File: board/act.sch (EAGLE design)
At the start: 27 parts, among them IC1 7805T, U1 ESP-WROOM-32, X3 DCJACK-MJ179P-R

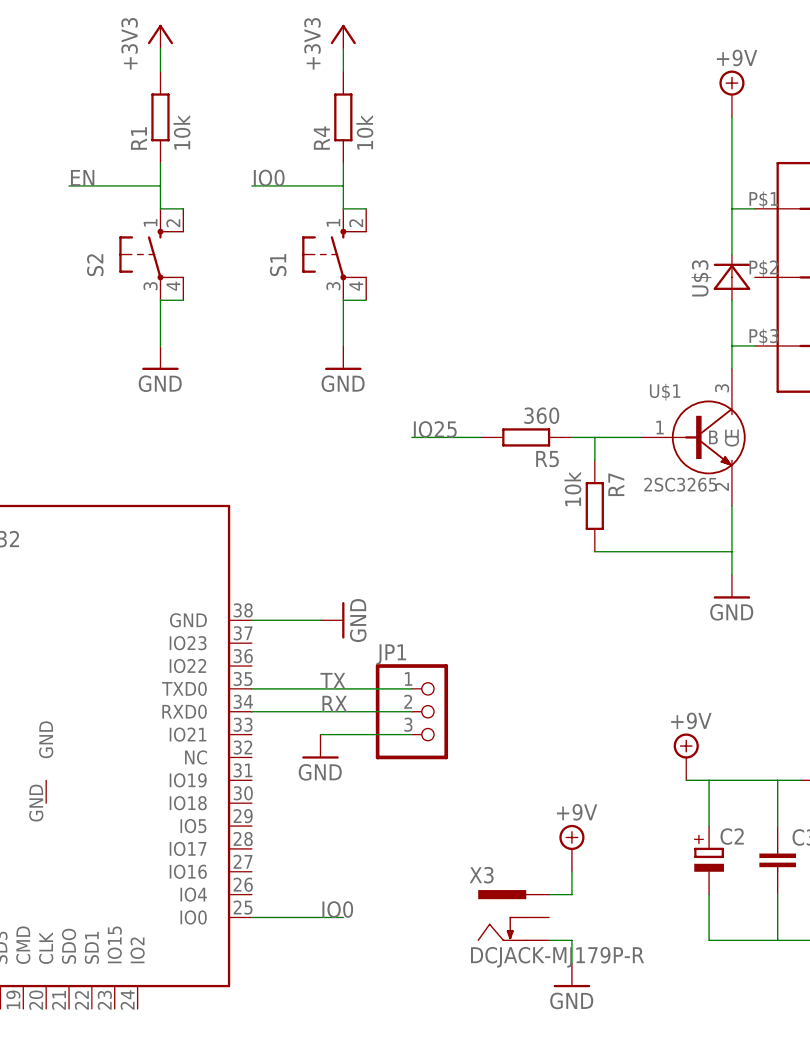
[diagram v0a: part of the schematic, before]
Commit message: add user_button
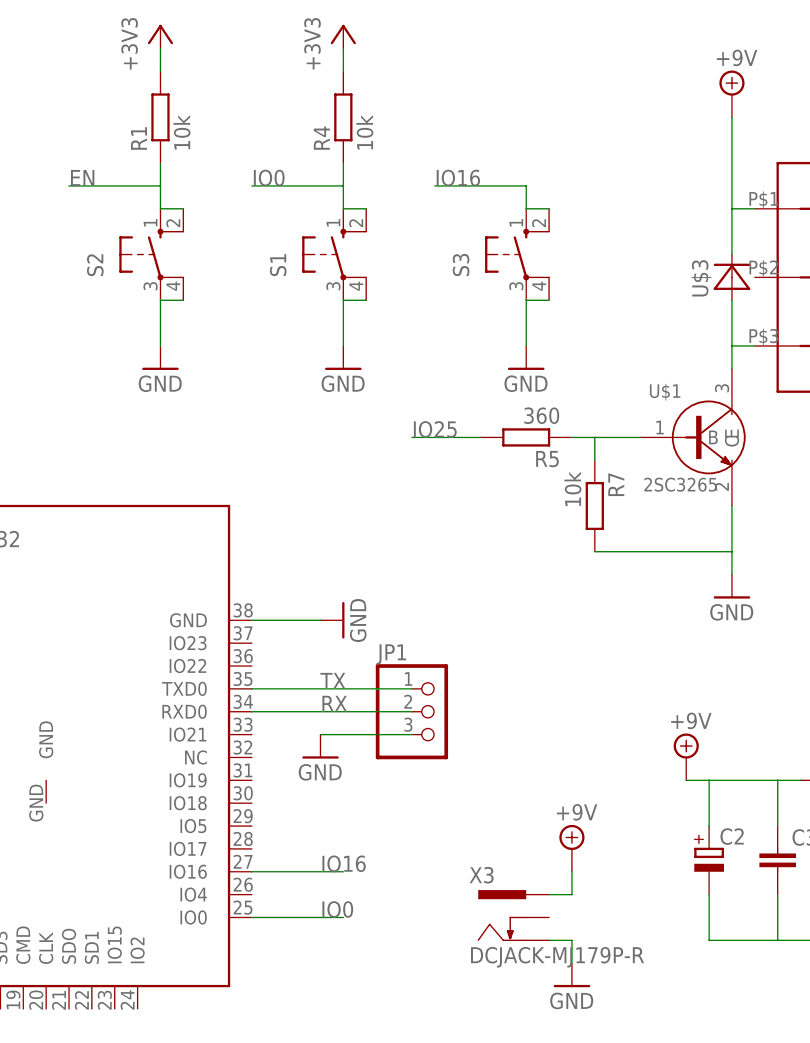
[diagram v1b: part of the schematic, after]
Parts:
- added S3: (no value), switch-omron:10-XX
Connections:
- new net IO16: S3.S, S3.S1, U1.IO16
- net GND: now also S3.P, S3.P1
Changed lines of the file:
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@@
 <part name="C2" library="rcl" deviceset="CPOL-EU" device="E5-4"/>
 <part name="C5" library="rcl" deviceset="CPOL-EU" device="E5-4"/>
+<part name="S3" library="switch-omron" deviceset="10-XX" device=""/>
+<part name="GND14" library="supply1" deviceset="GND" device=""/>
 </parts>
 <sheets>
@@
 <instance part="C2" gate="G$1" x="106.68" y="25.4"/>
 <instance part="C5" gate="G$1" x="144.78" y="25.4"/>
+<instance part="S3" gate="1" x="86.36" y="91.44"/>
+<instance part="GND14" gate="1" x="86.36" y="78.74"/>
 </instances>
 <busses>
@@
 <wire x1="63.5" y1="38.1" x2="73.66" y2="38.1" width="0.1524" layer="91"/>
 </segment>
+<segment>
+<pinref part="S3" gate="1" pin="P"/>
+<wire x1="86.36" y1="86.36" x2="86.36" y2="81.28" width="0.1524" layer="91"/>
+<pinref part="GND14" gate="1" pin="GND"/>
+<pinref part="S3" gate="1" pin="P1"/>
+<wire x1="86.36" y1="86.36" x2="88.9" y2="86.36" width="0.1524" layer="91"/>
+</segment>
 </net>
 <net name="+3V3" class="0">
@@
 </segment>
 </net>
+<net name="IO16" class="0">
+<segment>
+<pinref part="U1" gate="G$1" pin="IO16"/>
+<wire x1="55.88" y1="22.86" x2="66.04" y2="22.86" width="0.1524" layer="91"/>
+<label x="63.5" y="22.86" size="1.778" layer="95"/>
+</segment>
+<segment>
+<pinref part="S3" gate="1" pin="S"/>
+<wire x1="86.36" y1="96.52" x2="86.36" y2="99.06" width="0.1524" layer="91"/>
+<wire x1="86.36" y1="99.06" x2="76.2" y2="99.06" width="0.1524" layer="91"/>
+<label x="76.2" y="99.06" size="1.778" layer="95"/>
+<pinref part="S3" gate="1" pin="S1"/>
+<wire x1="86.36" y1="96.52" x2="88.9" y2="96.52" width="0.1524" layer="91"/>
+</segment>
+</net>
